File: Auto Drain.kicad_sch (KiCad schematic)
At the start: 67 parts, among them J1 AC, J2 Load 1, J3 Load 1, J4 Load 1, J5 ICSP, J6 Load 2, K1 RAYEX-L90A, Q1 2N3904, SW1 Options, T1 3FD-424, T2 CSE187L, T3 CSE187L, U1 LM7812_TO220, U2 LM1458, U3 LM7912_TO220, U4 LM1458, U5 LM7805_TO220, U6 PIC16F1829-ISS

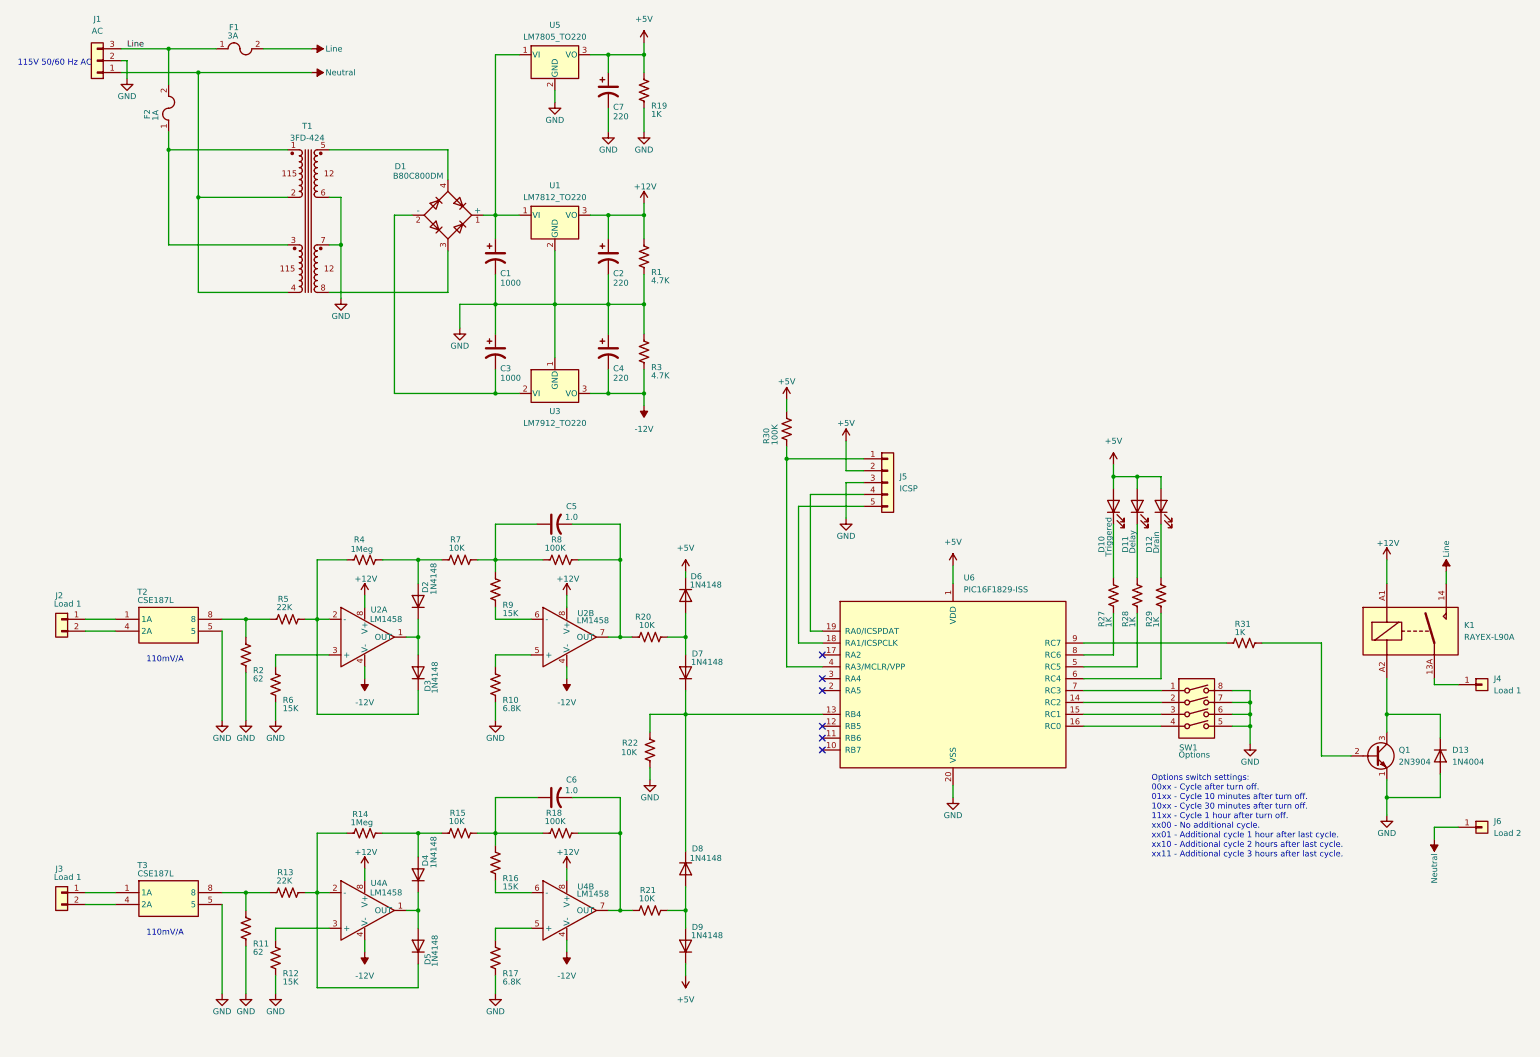
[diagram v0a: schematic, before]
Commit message: updates to use state machine
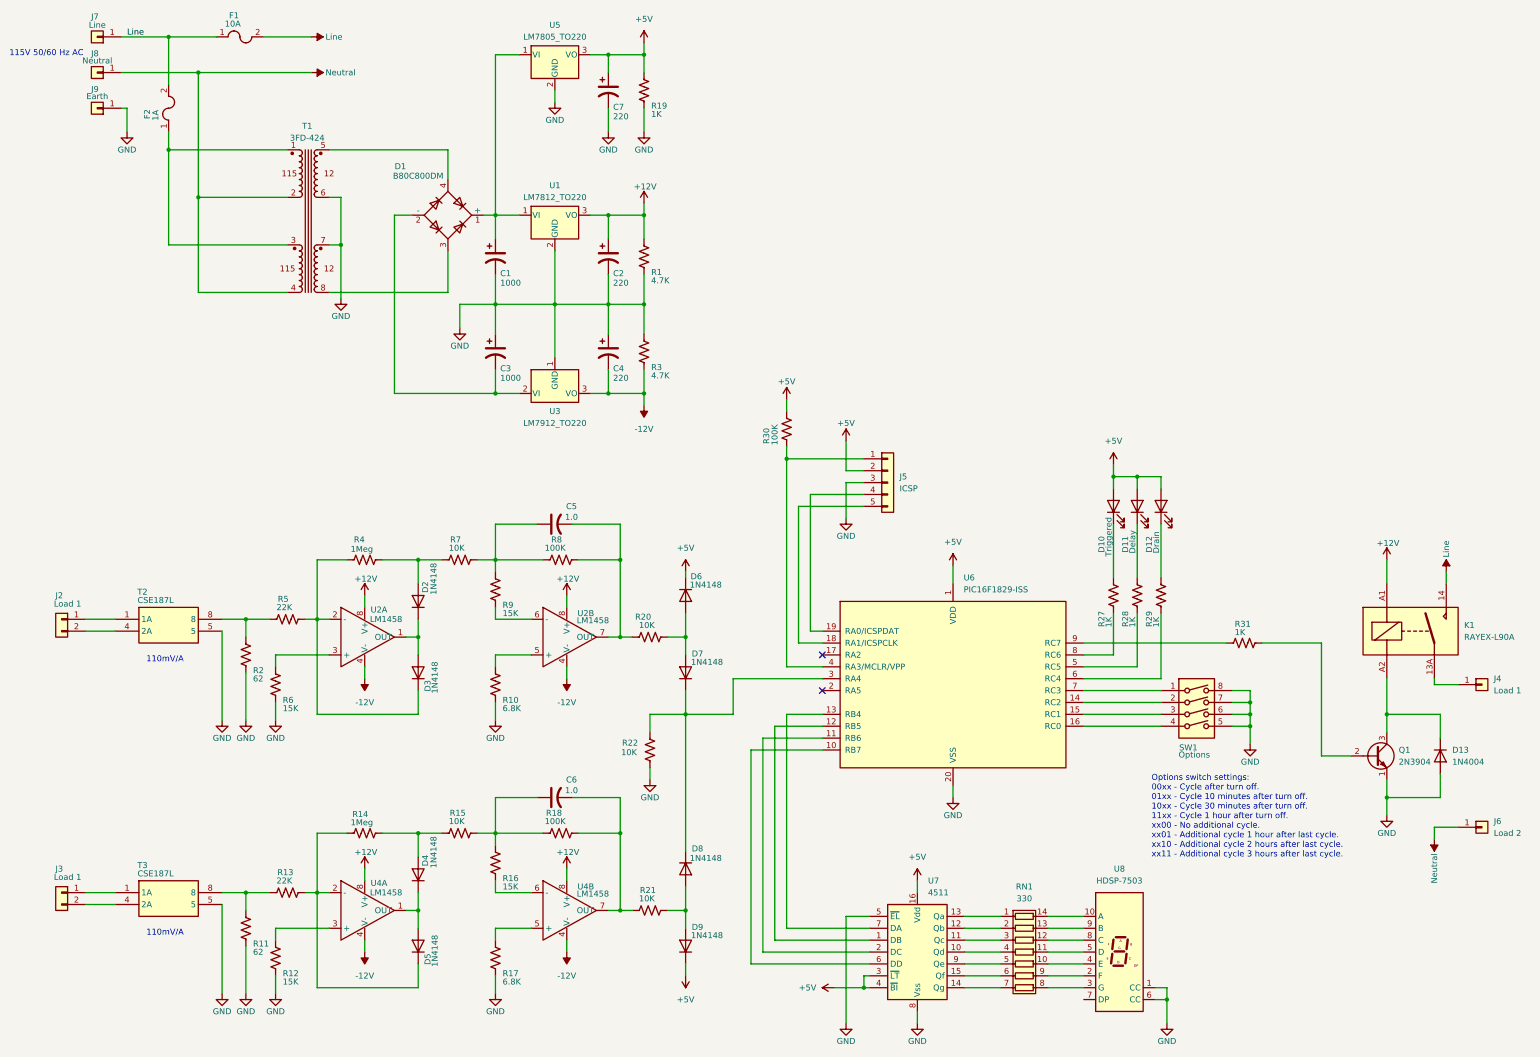
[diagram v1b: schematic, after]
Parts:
- removed J1: AC, Connector_TE-Connectivity:TE_MATE-N-LOK_1-770875-x_2x03_P4.14mm_Vertical, symbol Connector_Generic:Conn_01x03
- added J7: Line, DH_Hardware:Amp Faston 250 THT, symbol Connector_Generic:Conn_01x01
- added J8: Neutral, DH_Hardware:Amp Faston 250 THT, symbol Connector_Generic:Conn_01x01
- added J9: Earth, DH_Hardware:Amp Faston 250 THT, symbol Connector_Generic:Conn_01x01
- added RN1: 330, Package_DIP:DIP-8_W7.62mm, symbol Device:R_Pack07
- added U7: 4511, Package_DIP:DIP-14_W7.62mm, symbol 4xxx_IEEE:4511
- added U8: HDSP-7503, Display_7Segment:HDSP-A151, symbol Display_Character:HDSP-7503
- F1: value 3A -> 10A
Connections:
- net +5V: now also U7.16 (Vdd), U7.3 (~{LT}), U7.4 (~{BI})
- net GND: now also J9.1 (Pin_1), U7.5 (~{EL}), U7.8 (Vss), U8.1 (CC), U8.6 (CC)
- net Line: now also J7.1 (Pin_1)
- net Neutral: now also J8.1 (Pin_1)
- net at D7.1 (K), D8.1 (K), R22.2: now also U6.3 (RA4); no longer U6.13 (RB4)
- net at U6.10 (RB7): now also U7.6 (DD)
- net at U6.11 (RB6): now also U7.2 (DC)
- net at U6.12 (RB5): now also U7.1 (DB)
- new net: RN1.14 (R1.2), U8.10 (A)
- new net: RN1.9 (R6.2), U8.2 (F)
- new net: RN1.8 (R7.2), U8.3 (G)
- new net: RN1.10 (R5.2), U8.4 (E)
- new net: RN1.11 (R4.2), U8.5 (D)
- new net: RN1.12 (R3.2), U8.8 (C)
- new net: RN1.13 (R2.2), U8.9 (B)
- new net: RN1.1 (R1.1), U7.13 (Qa)
- new net: RN1.2 (R2.1), U7.12 (Qb)
- new net: RN1.3 (R3.1), U7.11 (Qc)
- new net: RN1.4 (R4.1), U7.10 (Qd)
- new net: RN1.5 (R5.1), U7.9 (Qe)
- new net: RN1.6 (R6.1), U7.15 (Qf)
- new net: RN1.7 (R7.1), U7.14 (Qg)
- new net: U6.13 (RB4), U7.7 (DA)
- no-connect marks 6 -> 2
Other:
- moved on the sheet: F1
